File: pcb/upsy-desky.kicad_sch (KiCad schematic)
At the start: 44 parts, among them J1 RJ45, J2 RJ45, J3 USB_C_ReceptacleUSB2.0, Q1 MMBT3904, Q2 MMBT3904, Q3 2N7002, Q4 2N7002, Q5 2N7002, Q6 2N7002, Q7 2N7002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

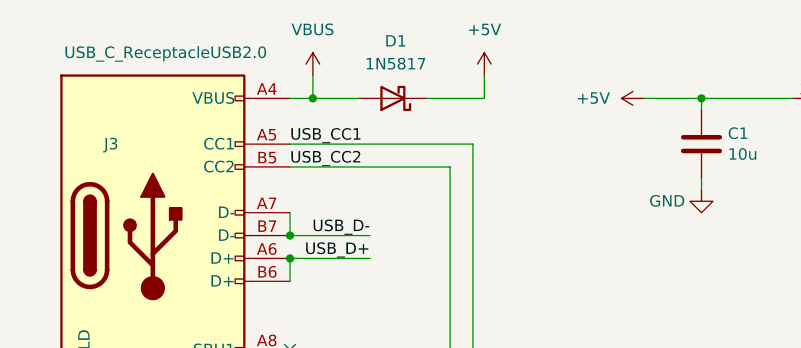
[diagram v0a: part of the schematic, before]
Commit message: Fix error in BOM - closes #45
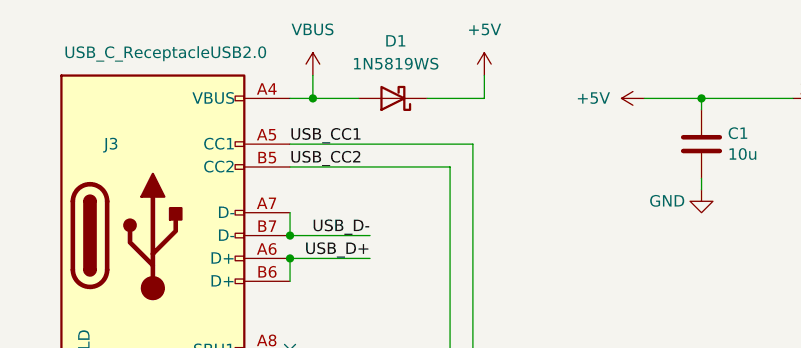
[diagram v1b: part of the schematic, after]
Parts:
- D1: value 1N5817 -> 1N5819WS; MPN 1N5817 -> 1N5819WS
- U1: MPN CP2102N-A02-GQFN24 -> CP2102N-Axx-xQFN28
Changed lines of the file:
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@@
       (effects (font (size 1.27 1.27)) hide)
     )
-    (property "MPN" "CP2102N-A02-GQFN24" (at 78.74 114.3 0)
+    (property "MPN" "CP2102N-Axx-xQFN28" (at 78.74 114.3 0)
       (effects (font (size 1.27 1.27)) hide)
     )
@@
       (effects (font (size 1.27 1.27)))
     )
-    (property "Value" "1N5817" (at 56.1975 19.05 0)
+    (property "Value" "1N5819WS" (at 56.1975 19.05 0)
       (effects (font (size 1.27 1.27)))
     )
@@
       (effects (font (size 1.27 1.27)) hide)
     )
-    (property "MPN" "1N5817" (at 55.88 22.86 0)
-      (effects (font (size 1.27 1.27)) hide)
-    )
+    (property "MPN" "1N5819WS" (at 55.88 22.86 0)
+      (effects (font (size 1.27 1.27)) hide)
+    )

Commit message: pcb: Update RJ45 part number
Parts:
- J1, J2: LCSC C708595 -> C3000202
